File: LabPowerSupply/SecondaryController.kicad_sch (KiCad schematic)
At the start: 22 parts, among them Y2 8M

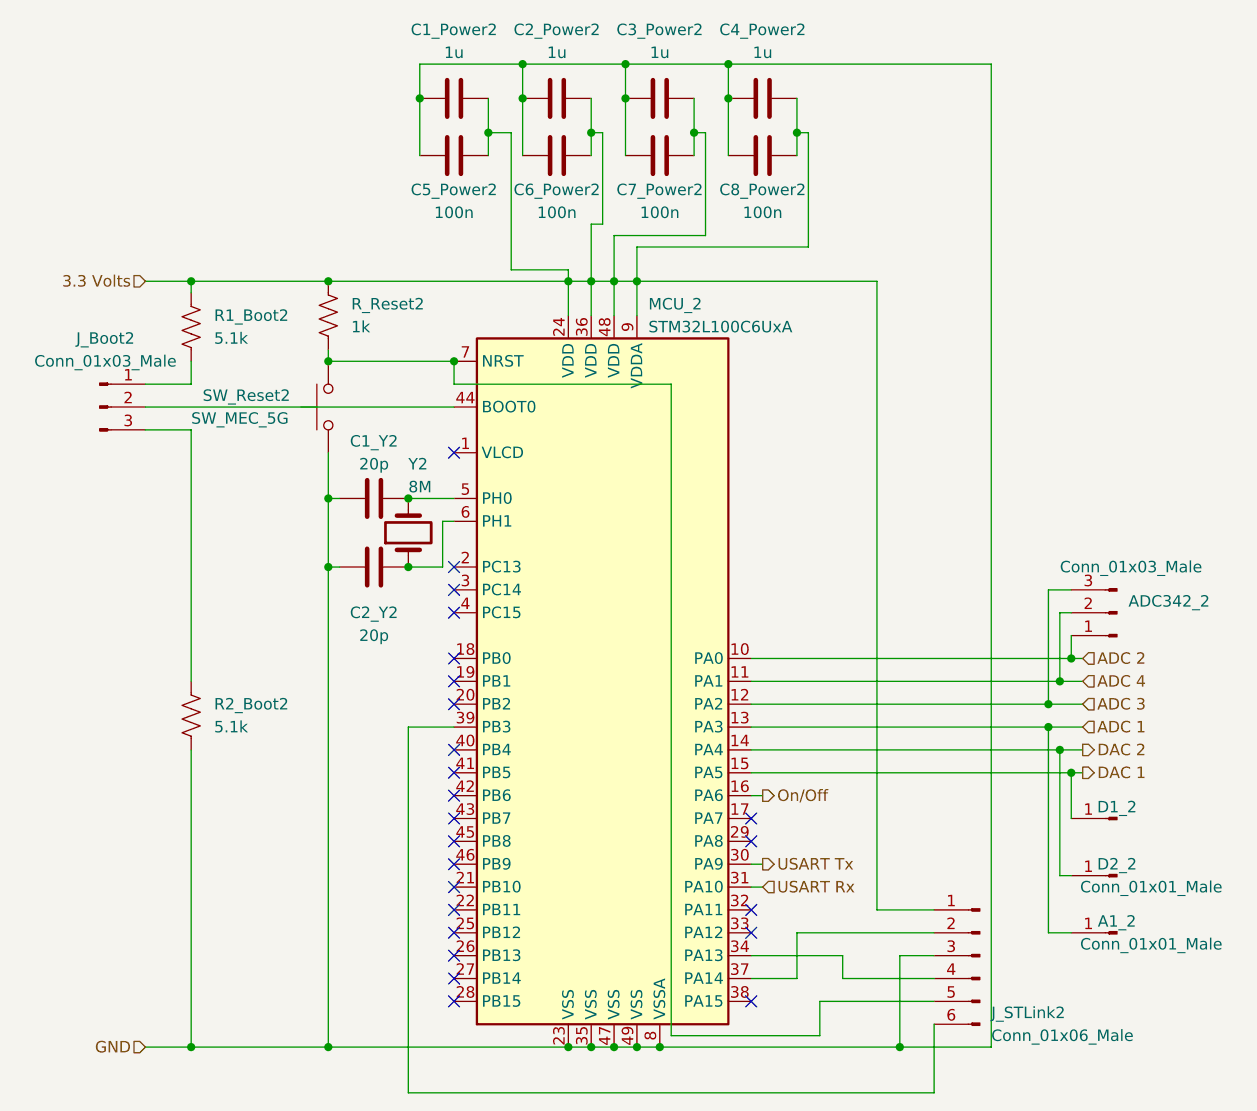
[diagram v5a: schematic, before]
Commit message: Updated Part List
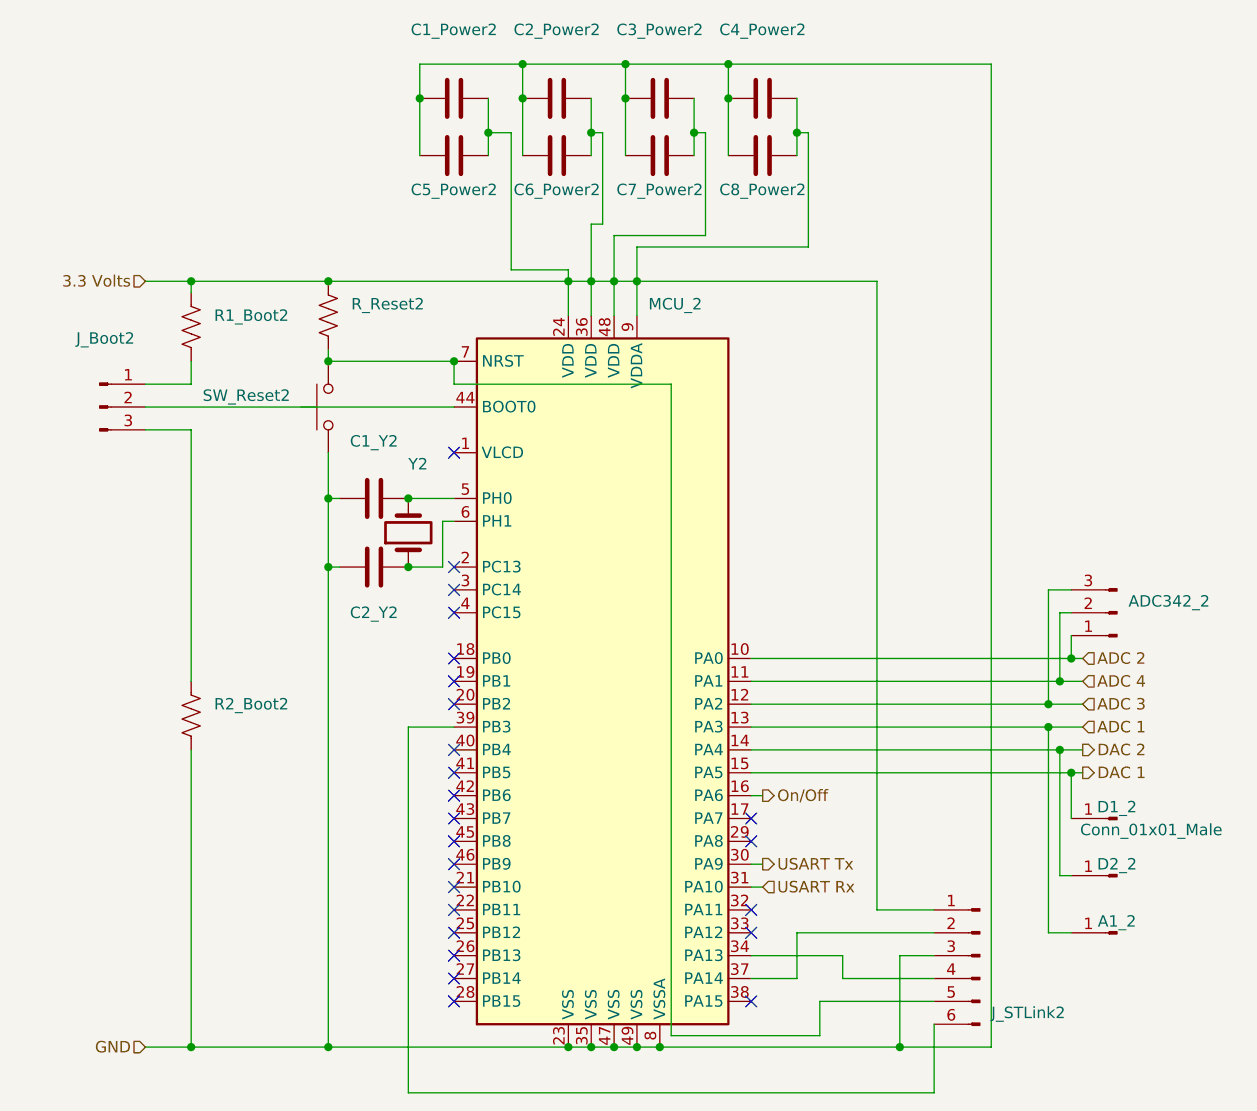
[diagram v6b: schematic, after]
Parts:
- A1_2, D2_2: value Conn_01x01_Male -> (none)
- ADC342_2: value Conn_01x03_Male -> (none); footprint Connector_PinHeader_2.54mm:PinHeader_1x03_P2.54mm_Vertical -> (none)
- C1_Power2, C2_Power2, C3_Power2, C4_Power2: value 1u -> (none); footprint Capacitor_SMD:C_0603_1608Metric -> (none)
- C1_Y2, C2_Y2: value 20p -> (none); footprint Capacitor_SMD:C_0603_1608Metric -> (none)
- C5_Power2, C6_Power2, C7_Power2, C8_Power2: value 100n -> (none); footprint Capacitor_SMD:C_0603_1608Metric -> (none)
- D1_2: value (none) -> Conn_01x01_Male
- J_Boot2: value Conn_01x03_Male -> (none)
- J_STLink2: value Conn_01x06_Male -> (none); footprint Connector_PinHeader_2.54mm:PinHeader_1x06_P2.54mm_Vertical -> (none)
- MCU_2: value STM32L100C6UxA -> (none); footprint Package_DFN_QFN:QFN-48-1EP_7x7mm_P0.5mm_EP5.6x5.6mm -> (none)
- R1_Boot2, R2_Boot2: value 5.1k -> (none); footprint Resistor_SMD:R_0603_1608Metric -> (none)
- R_Reset2: value 1k -> (none); footprint Resistor_SMD:R_0603_1608Metric -> (none)
- SW_Reset2: value SW_MEC_5G -> (none); footprint Button_Switch_THT:SW_PUSH-12mm -> (none)
- Y2: value 8M -> (none); footprint Crystal:Crystal_SMD_HC49-SD -> (none)
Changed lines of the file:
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@@
     (in_bom yes) (on_board yes)
     (property "Reference" "C8_Power2" (id 0) (at 116.84 44.45 90))
-    (property "Value" "100n" (id 1) (at 116.84 46.99 90))
-    (property "Footprint" "Capacitor_SMD:C_0603_1608Metric" (id 2) (at 120.65 39.6748 0)
+    (property "Value" "" (id 1) (at 116.84 46.99 90))
+    (property "Footprint" "" (id 2) (at 120.65 39.6748 0)
       (effects (font (size 1.27 1.27)) hide)
     )
@@
       (effects (font (size 1.27 1.27)) (justify right))
     )
-    (property "Value" "Conn_01x06_Male" (id 1) (at 142.24 138.43 0)
-      (effects (font (size 1.27 1.27)) (justify right))
-    )
-    (property "Footprint" "Connector_PinHeader_2.54mm:PinHeader_1x06_P2.54mm_Vertical" (id 2) (at 140.97 129.54 0)
+    (property "Value" "" (id 1) (at 142.24 138.43 0)
+      (effects (font (size 1.27 1.27)) (justify right))
+    )
+    (property "Footprint" "" (id 2) (at 140.97 129.54 0)
       (effects (font (size 1.27 1.27)) hide)
     )
@@
     (in_bom yes) (on_board yes)
     (property "Reference" "C2_Y2" (id 0) (at 73.66 91.44 90))
-    (property "Value" "20p" (id 1) (at 73.66 93.98 90))
-    (property "Footprint" "Capacitor_SMD:C_0603_1608Metric" (id 2) (at 77.47 87.3252 0)
+    (property "Value" "" (id 1) (at 73.66 93.98 90))
+    (property "Footprint" "" (id 2) (at 77.47 87.3252 0)
       (effects (font (size 1.27 1.27)) hide)
     )
@@
       (effects (font (size 1.27 1.27)) (justify left))
     )
-    (property "Value" "5.1k" (id 1) (at 55.88 60.9599 0)
-      (effects (font (size 1.27 1.27)) (justify left))
-    )
-    (property "Footprint" "Resistor_SMD:R_0603_1608Metric" (id 2) (at 54.356 59.944 90)
+    (property "Value" "" (id 1) (at 55.88 60.9599 0)
+      (effects (font (size 1.27 1.27)) (justify left))
+    )
+    (property "Footprint" "" (id 2) (at 54.356 59.944 90)
       (effects (font (size 1.27 1.27)) hide)
     )
@@
     (in_bom yes) (on_board yes)
     (property "Reference" "C7_Power2" (id 0) (at 105.41 44.45 90))
-    (property "Value" "100n" (id 1) (at 105.41 46.99 90))
-    (property "Footprint" "Capacitor_SMD:C_0603_1608Metric" (id 2) (at 109.22 39.6748 0)
+    (property "Value" "" (id 1) (at 105.41 46.99 90))
+    (property "Footprint" "" (id 2) (at 109.22 39.6748 0)
       (effects (font (size 1.27 1.27)) hide)
     )
@@
       (effects (font (size 1.27 1.27)) (justify left))
     )
-    (property "Value" "5.1k" (id 1) (at 55.88 104.1399 0)
-      (effects (font (size 1.27 1.27)) (justify left))
-    )
-    (property "Footprint" "Resistor_SMD:R_0603_1608Metric" (id 2) (at 54.356 103.124 90)
+    (property "Value" "" (id 1) (at 55.88 104.1399 0)
+      (effects (font (size 1.27 1.27)) (justify left))
+    )
+    (property "Footprint" "" (id 2) (at 54.356 103.124 90)
       (effects (font (size 1.27 1.27)) hide)
     )
@@
     (in_bom yes) (on_board yes) (fields_autoplaced)
     (property "Reference" "J_Boot2" (id 0) (at 43.815 60.96 0))
-    (property "Value" "Conn_01x03_Male" (id 1) (at 43.815 63.5 0))
+    (property "Value" "" (id 1) (at 43.815 63.5 0))
     (property "Footprint" "" (id 2) (at 43.18 68.58 0)
       (effects (font (size 1.27 1.27)) hide)
@@
       (effects (font (size 1.27 1.27)) (justify left))
     )
-    (property "Value" "STM32L100C6UxA" (id 1) (at 104.14 59.69 0)
-      (effects (font (size 1.27 1.27)) (justify left))
-    )
-    (property "Footprint" "Package_DFN_QFN:QFN-48-1EP_7x7mm_P0.5mm_EP5.6x5.6mm" (id 2) (at 85.09 137.16 0)
+    (property "Value" "" (id 1) (at 104.14 59.69 0)
+      (effects (font (size 1.27 1.27)) (justify left))
+    )
+    (property "Footprint" "" (id 2) (at 85.09 137.16 0)
       (effects (font (size 1.27 1.27)) (justify right) hide)
     )
@@
     (in_bom yes) (on_board yes) (fields_autoplaced)
     (property "Reference" "C1_Power2" (id 0) (at 82.55 26.67 90))
-    (property "Value" "1u" (id 1) (at 82.55 29.21 90))
-    (property "Footprint" "Capacitor_SMD:C_0603_1608Metric" (id 2) (at 86.36 33.3248 0)
+    (property "Value" "" (id 1) (at 82.55 29.21 90))
+    (property "Footprint" "" (id 2) (at 86.36 33.3248 0)
       (effects (font (size 1.27 1.27)) hide)
     )
@@
     (in_bom yes) (on_board yes)
     (property "Reference" "C5_Power2" (id 0) (at 82.55 44.45 90))
-    (property "Value" "100n" (id 1) (at 82.55 46.99 90))
-    (property "Footprint" "Capacitor_SMD:C_0603_1608Metric" (id 2) (at 86.36 39.6748 0)
+    (property "Value" "" (id 1) (at 82.55 46.99 90))
+    (property "Footprint" "" (id 2) (at 86.36 39.6748 0)
       (effects (font (size 1.27 1.27)) hide)
     )
@@
       (effects (font (size 1.27 1.27)) (justify right))
     )
-    (property "Value" "Conn_01x03_Male" (id 1) (at 149.86 86.36 0)
-      (effects (font (size 1.27 1.27)) (justify right))
-    )
-    (property "Footprint" "Connector_PinHeader_2.54mm:PinHeader_1x03_P2.54mm_Vertical" (id 2) (at 156.21 91.44 0)
+    (property "Value" "" (id 1) (at 149.86 86.36 0)
+      (effects (font (size 1.27 1.27)) (justify right))
+    )
+    (property "Footprint" "" (id 2) (at 156.21 91.44 0)
       (effects (font (size 1.27 1.27)) hide)
     )
@@
     (in_bom yes) (on_board yes)
     (property "Reference" "C6_Power2" (id 0) (at 93.98 44.45 90))
-    (property "Value" "100n" (id 1) (at 93.98 46.99 90))
-    (property "Footprint" "Capacitor_SMD:C_0603_1608Metric" (id 2) (at 97.79 39.6748 0)
+    (property "Value" "" (id 1) (at 93.98 46.99 90))
+    (property "Footprint" "" (id 2) (at 97.79 39.6748 0)
       (effects (font (size 1.27 1.27)) hide)
     )
@@
     (in_bom yes) (on_board yes)
     (property "Reference" "D2_2" (id 0) (at 156.21 119.38 0))
-    (property "Value" "Conn_01x01_Male" (id 1) (at 160.02 121.92 0))
+    (property "Value" "" (id 1) (at 160.02 121.92 0))
     (property "Footprint" "" (id 2) (at 156.21 120.65 0)
       (effects (font (size 1.27 1.27)) hide)
@@
     (in_bom yes) (on_board yes) (fields_autoplaced)
     (property "Reference" "C2_Power2" (id 0) (at 93.98 26.67 90))
-    (property "Value" "1u" (id 1) (at 93.98 29.21 90))
-    (property "Footprint" "Capacitor_SMD:C_0603_1608Metric" (id 2) (at 97.79 33.3248 0)
+    (property "Value" "" (id 1) (at 93.98 29.21 90))
+    (property "Footprint" "" (id 2) (at 97.79 33.3248 0)
       (effects (font (size 1.27 1.27)) hide)
     )
@@
     (in_bom yes) (on_board yes)
     (property "Reference" "C1_Y2" (id 0) (at 73.66 72.39 90))
-    (property "Value" "20p" (id 1) (at 73.66 74.93 90))
-    (property "Footprint" "Capacitor_SMD:C_0603_1608Metric" (id 2) (at 77.47 77.7748 0)
+    (property "Value" "" (id 1) (at 73.66 74.93 90))
+    (property "Footprint" "" (id 2) (at 77.47 77.7748 0)
       (effects (font (size 1.27 1.27)) hide)
     )
@@
       (effects (font (size 1.27 1.27)) (justify right))
     )
-    (property "Value" "SW_MEC_5G" (id 1) (at 53.34 69.85 90)
-      (effects (font (size 1.27 1.27)) (justify right))
-    )
-    (property "Footprint" "Button_Switch_THT:SW_PUSH-12mm" (id 2) (at 63.5 68.58 0)
+    (property "Value" "" (id 1) (at 53.34 69.85 90)
+      (effects (font (size 1.27 1.27)) (justify right))
+    )
+    (property "Footprint" "" (id 2) (at 63.5 68.58 0)
       (effects (font (size 1.27 1.27)) hide)
     )
@@
     (in_bom yes) (on_board yes) (fields_autoplaced)
     (property "Reference" "C3_Power2" (id 0) (at 105.41 26.67 90))
-    (property "Value" "1u" (id 1) (at 105.41 29.21 90))
-    (property "Footprint" "Capacitor_SMD:C_0603_1608Metric" (id 2) (at 109.22 33.3248 0)
+    (property "Value" "" (id 1) (at 105.41 29.21 90))
+    (property "Footprint" "" (id 2) (at 109.22 33.3248 0)
       (effects (font (size 1.27 1.27)) hide)
     )
@@
     (in_bom yes) (on_board yes)
     (property "Reference" "A1_2" (id 0) (at 156.21 125.73 0))
-    (property "Value" "Conn_01x01_Male" (id 1) (at 160.02 128.27 0))
+    (property "Value" "" (id 1) (at 160.02 128.27 0))
     (property "Footprint" "" (id 2) (at 156.21 127 0)
       (effects (font (size 1.27 1.27)) hide)
@@
       (effects (font (size 1.27 1.27)) (justify right))
     )
-    (property "Value" "8M" (id 1) (at 77.47 77.47 90)
-      (effects (font (size 1.27 1.27)) (justify right))
-    )
-    (property "Footprint" "Crystal:Crystal_SMD_HC49-SD" (id 2) (at 77.47 82.55 0)
+    (property "Value" "" (id 1) (at 77.47 77.47 90)
+      (effects (font (size 1.27 1.27)) (justify right))
+    )
+    (property "Footprint" "" (id 2) (at 77.47 82.55 0)
       (effects (font (size 1.27 1.27)) hide)
     )
@@
     (in_bom yes) (on_board yes) (fields_autoplaced)
     (property "Reference" "C4_Power2" (id 0) (at 116.84 26.67 90))
-    (property "Value" "1u" (id 1) (at 116.84 29.21 90))
-    (property "Footprint" "Capacitor_SMD:C_0603_1608Metric" (id 2) (at 120.65 33.3248 0)
+    (property "Value" "" (id 1) (at 116.84 29.21 90))
+    (property "Footprint" "" (id 2) (at 120.65 33.3248 0)
       (effects (font (size 1.27 1.27)) hide)
     )
@@
       (effects (font (size 1.27 1.27)) (justify left))
     )
-    (property "Value" "1k" (id 1) (at 71.12 59.6899 0)
-      (effects (font (size 1.27 1.27)) (justify left))
-    )
-    (property "Footprint" "Resistor_SMD:R_0603_1608Metric" (id 2) (at 69.596 58.674 90)
+    (property "Value" "" (id 1) (at 71.12 59.6899 0)
+      (effects (font (size 1.27 1.27)) (justify left))
+    )
+    (property "Footprint" "" (id 2) (at 69.596 58.674 90)
       (effects (font (size 1.27 1.27)) hide)
     )
@@
     (in_bom yes) (on_board yes)
     (property "Reference" "D1_2" (id 0) (at 156.21 113.03 0))
-    (property "Value" "" (id 1) (at 160.02 115.57 0))
+    (property "Value" "Conn_01x01_Male" (id 1) (at 160.02 115.57 0))
     (property "Footprint" "" (id 2) (at 156.21 114.3 0)
       (effects (font (size 1.27 1.27)) hide)
